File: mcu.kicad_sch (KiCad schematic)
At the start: 21 parts, among them J301 GPIO, SW301 RST, SW302 BOOT0, U301 STM32G0B1KBUx

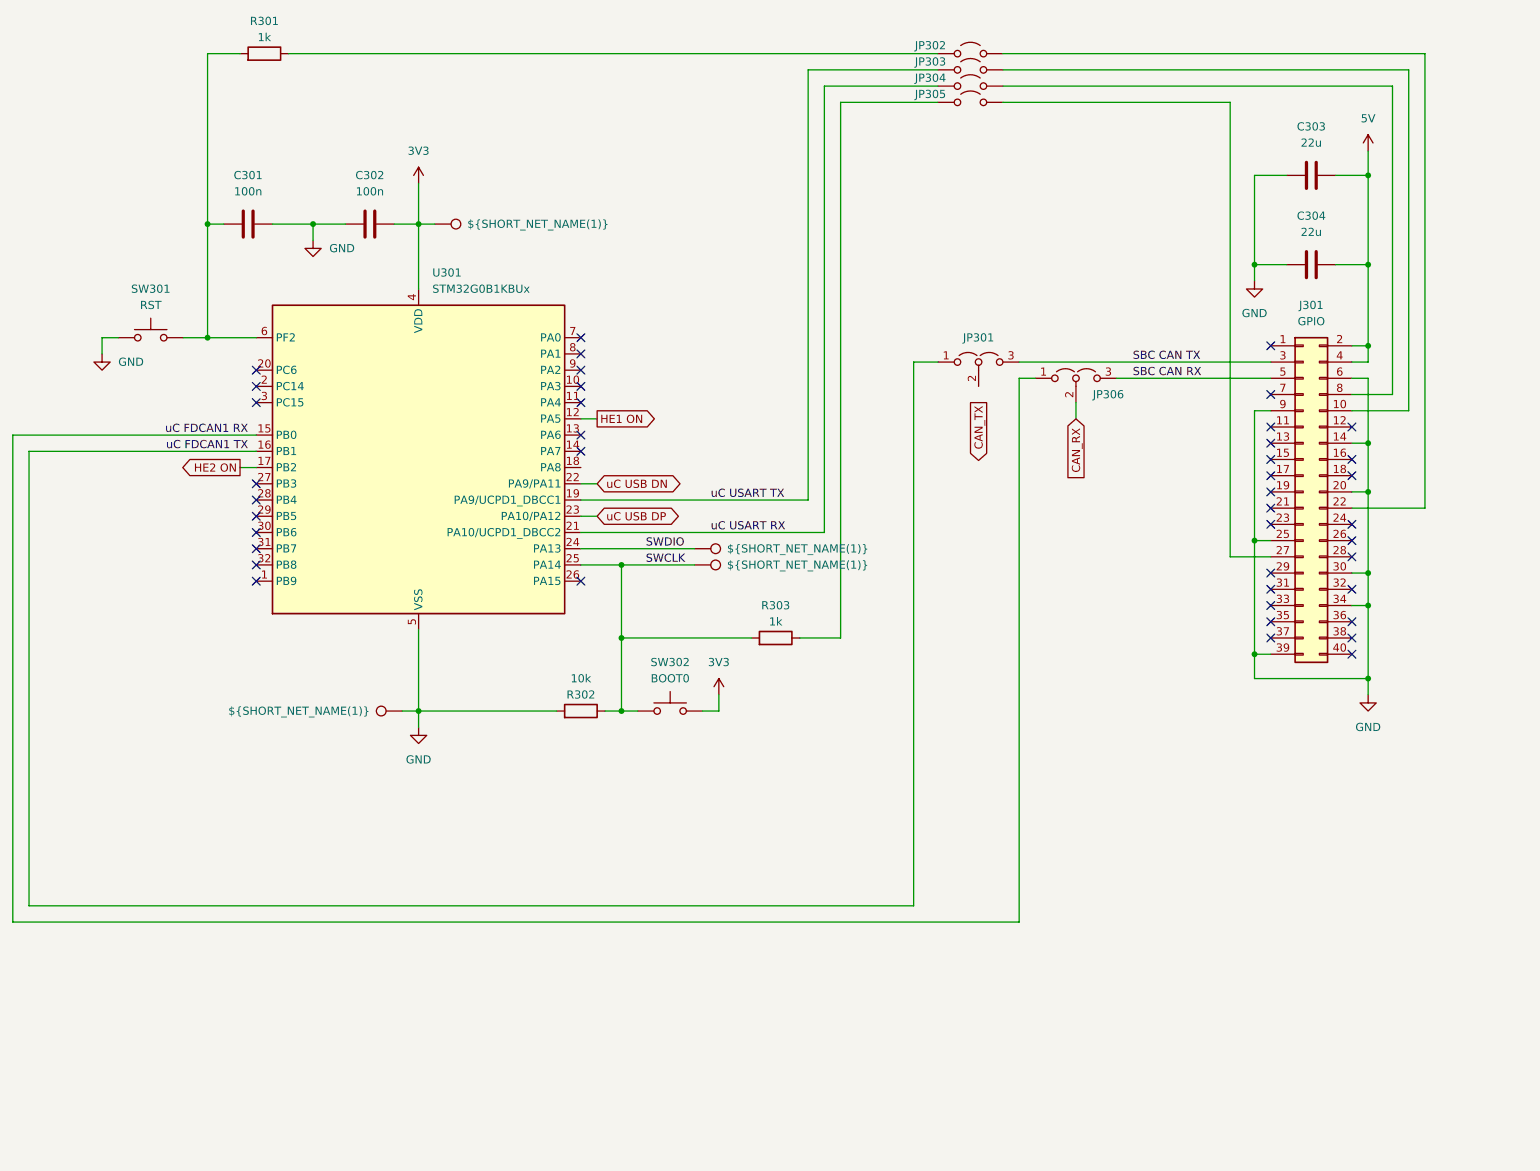
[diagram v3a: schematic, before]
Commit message: Schema improvements and CAN transceiver modification
- Improved schema layout for better readability and organization
- Connected CAN transceiver S-pin to GND for proper operation
- Updated PCB layout to reflect schema changes
- Enhanced component placement and routing clarity
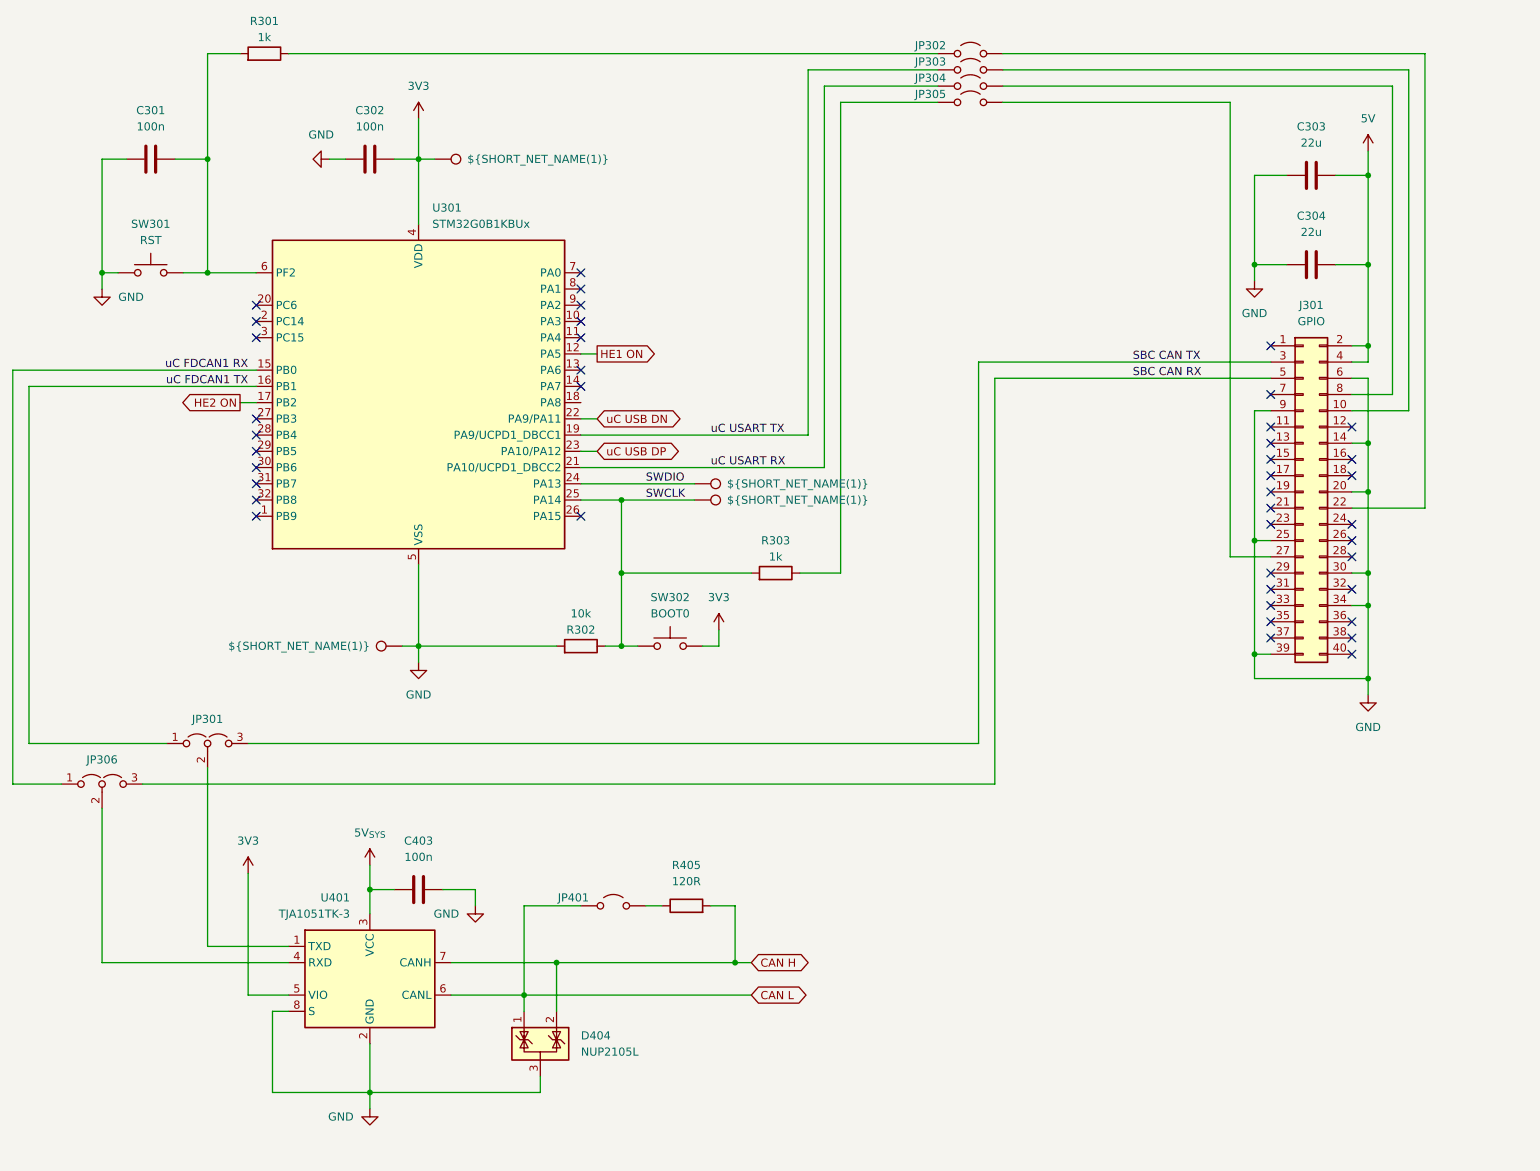
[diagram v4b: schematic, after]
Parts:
- added C403: 100n, Capacitor_SMD:C_0402_1005Metric, symbol Device:C
- added D404: NUP2105L, Package_TO_SOT_SMD:SOT-23, symbol Power_Protection:NUP2105L
- added JP401: ~, Connector_PinHeader_2.54mm:PinHeader_1x02_P2.54mm_Vertical, symbol Jumper:Jumper_2_Open
- added R405: 120R, Resistor_SMD:R_0402_1005Metric_Pad0.72x0.64mm_HandSolder, symbol Device:R
- added U401: TJA1051TK-3, Package_SON:HVSON-8-1EP_3x3mm_P0.65mm_EP1.6x2.4mm, symbol Interface_CAN_LIN:TJA1051TK-3
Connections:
- net 3V3: now also U401.5 (VIO)
- net GND: now also C403.1, D404.3 (A), U401.2 (GND), U401.8 (S), U401.9 (GND)
- net at JP301.2 (C): now also U401.1 (TXD)
- net CAN_RX: no longer names the net of JP306.2 (C)
- net CAN_RX: now also U401.4 (RXD)
- new net: JP401.2 (B), R405.1
- new net 5V_{SYS}: C403.2, U401.3 (VCC)
- new net CAN H: D404.2 (K), R405.2, U401.7 (CANH)
- new net CAN L: D404.1 (K), JP401.1 (A), U401.6 (CANL)
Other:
- moved on the sheet: C301, C302, JP301, JP306, R302, R303, SW301, SW302, U301

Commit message: Rev 0.2: Major hardware improvements and production readiness
Hardware Improvements (Thanks to shx for schematic cleanup):
- Clean up schematic organization and structure
- Set CAN transceiver Silent pin to GND for stability
- Add status LEDs (yellow: 24V/5V/3.3V, green: MCU PB4)
- Replace jumpers with solder jumpers on bottom side
- Add jumpers to output PFETs for permanent-on without firmware
- Add robust test points for 5V/GND load testing
- Add optional heatsink for DC/DC converter on bottom
- Add 10µF capacitor for MCU on 3.3V rail

Component Optimizations:
- Replace 30kΩ with 33kΩ basic part for simplified BOM
- Change DC/DC feedback: 15.5kΩ15kΩ (new output: 5.1V)
- Upgrade CAN ESD protection: NUP2105LPESD1CAN
- Increase CAN termination resistor footprint: 04020603
- Switch USB hub supply from 5V to 3.3V per datasheet

Production Ready:
- Add all LCSC part numbers and rotations
- Generate complete production data package
- Improve PCB layout and button placement
- Create comprehensive changelog documentation
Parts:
- removed TP302: ${SHORT_NET_NAME(1)}, project:NAMED_TEST_POINT, symbol project:NamedTestPoint
- added C303: 10u, Capacitor_SMD:C_0603_1608Metric, symbol Device:C
- added D301: GREEN, LED_SMD:LED_0805_2012Metric, symbol Device:LED
- added R301: 330R, Resistor_SMD:R_0402_1005Metric, symbol Device:R
- C301, C302: LCSC Part # (none) -> C307331; Manufacturer Part # (none) -> CL05B104KB54PNC
- C304: renamed from C403; LCSC Part # (none) -> C307331; Manufacturer Part # (none) -> CL05B104KB54PNC
- C305: renamed from C303; LCSC Part # (none) -> C12891; Manufacturer Part # (none) -> CL31A226KAHNNNE
- C306: renamed from C304; LCSC Part # (none) -> C12891; Manufacturer Part # (none) -> CL31A226KAHNNNE
- D302: renamed from D404; value NUP2105L -> PESD1CAN; LCSC Part # (none) -> C907838; Manufacturer Part # (none) -> PESD1CAN
- JP301: renamed from JP306; value Jumper_3_Open -> ~; footprint Connector_PinHeader_2.54mm:PinHeader_1x03_P2.54mm_Vertical -> project:SolderJumper-3_P1.3mm_Bridged12_RoundedPad1.0x1.5mm_custom; symbol Jumper:Jumper_3_Open -> Jumper:Jumper_3_Bridged12
- JP302: renamed from JP301; value Jumper_3_Open -> ~; footprint Connector_PinHeader_2.54mm:PinHeader_1x03_P2.54mm_Vertical -> project:SolderJumper-3_P1.3mm_Bridged12_RoundedPad1.0x1.5mm_custom; symbol Jumper:Jumper_3_Open -> Jumper:Jumper_3_Bridged12
- JP303: renamed from JP401; footprint Connector_PinHeader_2.54mm:PinHeader_1x02_P2.54mm_Vertical -> Jumper:SolderJumper-2_P1.3mm_Open_RoundedPad1.0x1.5mm; now left out of the parts list
- JP304: renamed from JP302; footprint Connector_PinHeader_2.54mm:PinHeader_1x02_P2.54mm_Vertical -> Jumper:SolderJumper-2_P1.3mm_Open_RoundedPad1.0x1.5mm; now left out of the parts list
- JP305: renamed from JP303; footprint Connector_PinHeader_2.54mm:PinHeader_1x02_P2.54mm_Vertical -> Jumper:SolderJumper-2_P1.3mm_Open_RoundedPad1.0x1.5mm; now left out of the parts list
- JP306: renamed from JP304; footprint Connector_PinHeader_2.54mm:PinHeader_1x02_P2.54mm_Vertical -> Jumper:SolderJumper-2_P1.3mm_Open_RoundedPad1.0x1.5mm; now left out of the parts list
- JP307: renamed from JP305; footprint Connector_PinHeader_2.54mm:PinHeader_1x02_P2.54mm_Vertical -> Jumper:SolderJumper-2_P1.3mm_Open_RoundedPad1.0x1.5mm; now left out of the parts list
- R302: renamed from R301; LCSC Part # (none) -> C11702; Manufacturer Part # (none) -> 0402WGF1001TCE
- R303: renamed from R302; LCSC Part # (none) -> C25744; Manufacturer Part # (none) -> 0402WGF1002TCE
- R304: renamed from R405; footprint Resistor_SMD:R_0402_1005Metric_Pad0.72x0.64mm_HandSolder -> Resistor_SMD:R_0603_1608Metric; LCSC Part # (none) -> C22787; Manufacturer Part # (none) -> 0603WAF1200T5E
- R305: renamed from R303; LCSC Part # (none) -> C11702; Manufacturer Part # (none) -> 0402WGF1001TCE
- SW301: value RST -> TS-1088; LCSC Part # (none) -> C720477; Manufacturer Part # (none) -> TS-1088-AR02016
- SW302: value BOOT0 -> TS-1088; LCSC Part # (none) -> C720477; Manufacturer Part # (none) -> TS-1088-AR02016
- TP301: now left out of the parts list
- TP302: renamed from TP303; now left out of the parts list
- TP303: renamed from TP304; now left out of the parts list
- U301: renamed from U401; LCSC Part # (none) -> C2875699; Manufacturer Part # (none) -> TJA1051TK/3/1J
- U302: renamed from U301; FT Rotation Offset (none) -> 270; LCSC Part # (none) -> C5159549; Manufacturer Part # (none) -> STM32G0B1KBU6
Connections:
- net 3V3: now also C303.1
- net GND: now also C303.2, D301.1 (K)
- net HE1 ON: now also U302.18 (PA8); no longer U302.12 (PA5)
- net at U302.28 (PB4): now also R301.1
- new net: D301.2 (A), R301.2
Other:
- moved on the sheet: C302

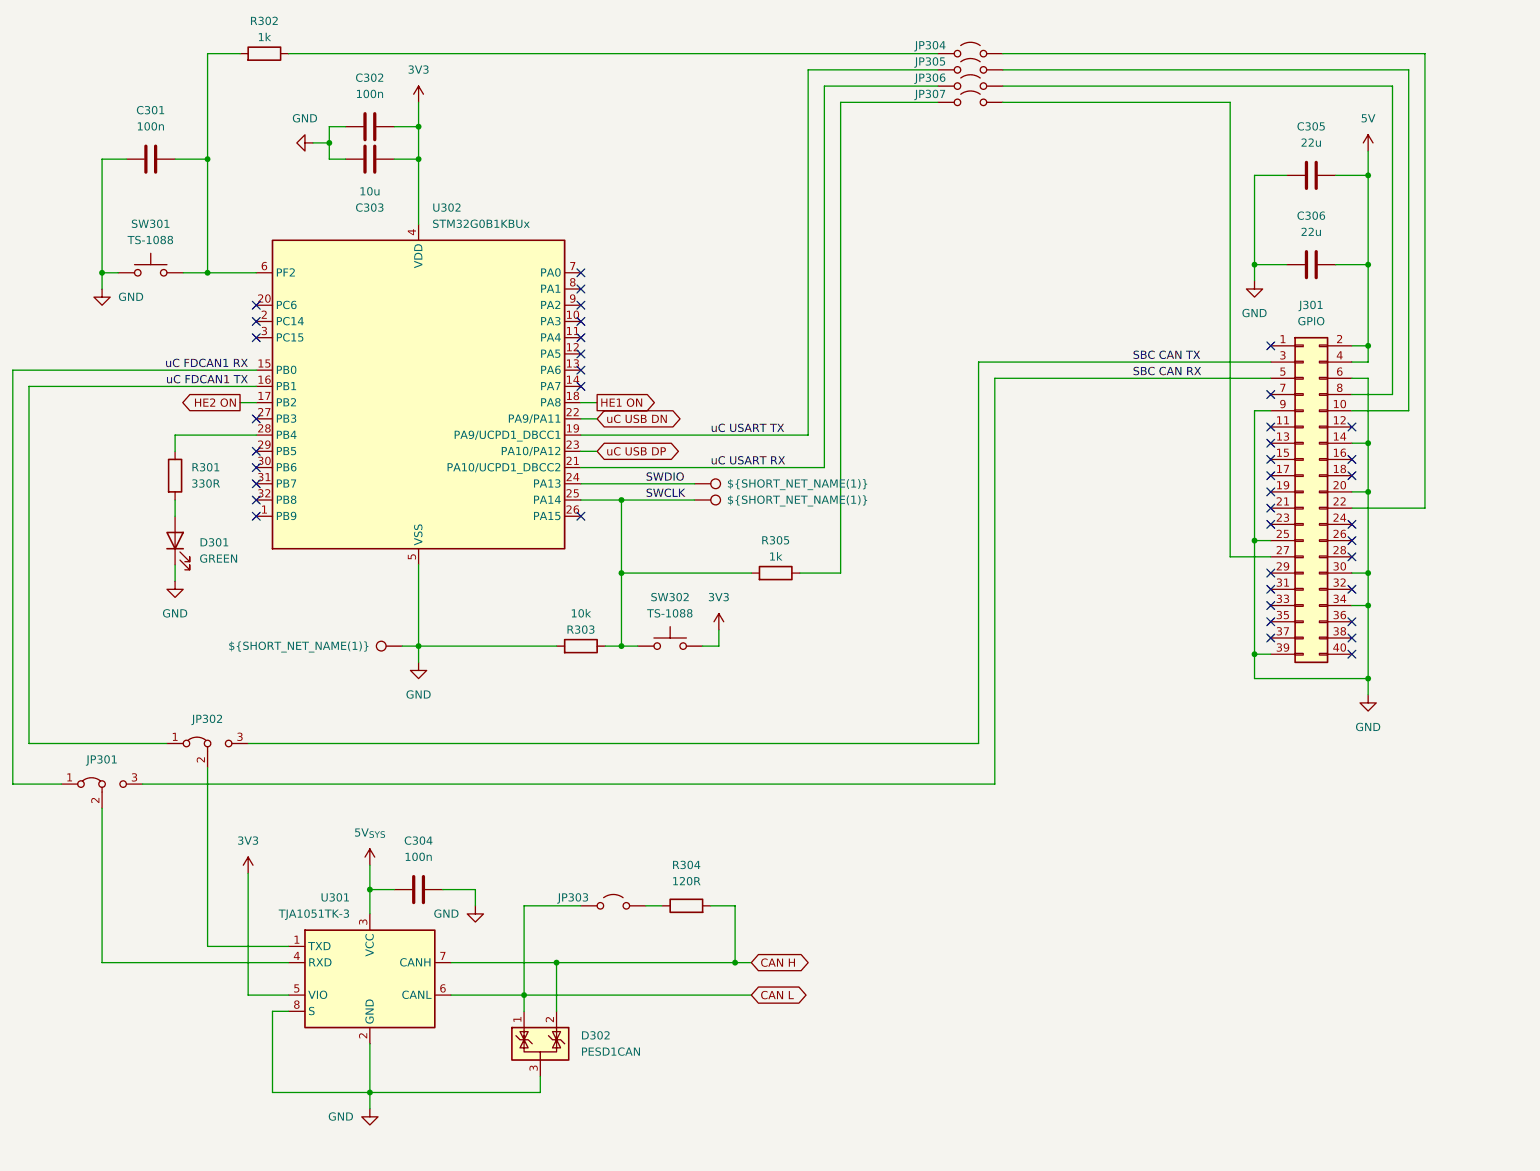
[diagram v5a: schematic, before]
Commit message: Rev. 0.3: Add 10µF capacitor C304 to CAN transceiver and QR code placeholder
- Added 10µF capacitor C304 for improved CAN communication stability
- Added QR code placeholder for serial number on PCB
- Enhanced signal integrity with additional filtering at CAN transceiver
- Improved traceability with unique identification capability
- Updated changelogs and documentation for Rev. 0.3
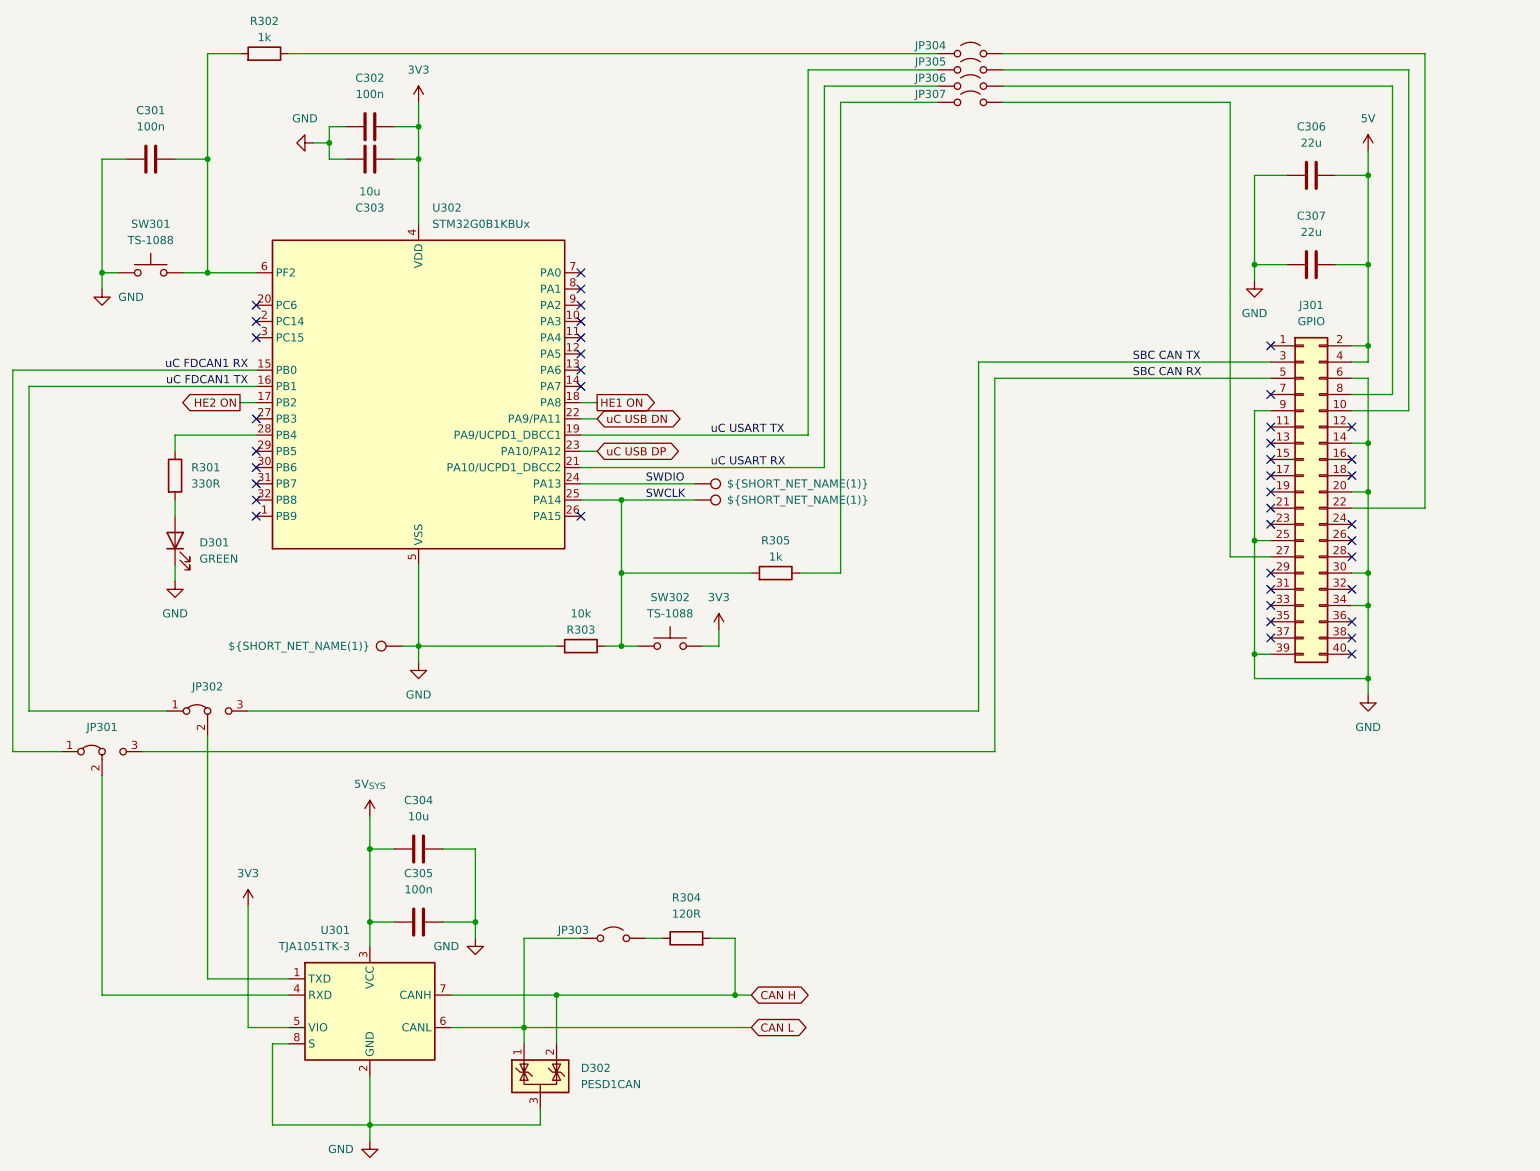
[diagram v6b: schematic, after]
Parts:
- added C304: 10u, Capacitor_SMD:C_0603_1608Metric, symbol Device:C
- renumbered C304 to C305, C305 to C306, C306 to C307
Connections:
- net 5V_{SYS}: now also C304.1
- net GND: now also C304.2
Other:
- moved on the sheet: C305, D302, JP301, JP302, JP303, R304, U301

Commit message: Production Optimization: JLCPCB assembly improvements
- Excluded test points TP202/TP203 from BOM
- Set FT rotation offsets for automated assembly:
  - U202/U301: 270° rotation offset
  - U401: 180° rotation offset
- Updated production data for JLCPCB compatibility
- Added unreleased changelog section for tracking
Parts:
- U301: FT Rotation Offset (none) -> 270
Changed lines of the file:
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@@
+			)
+		)
+		(property "FT Rotation Offset" "270"
+			(at 95.25 172.72 0)
+			(effects
+				(font
+					(size 1.27 1.27)
+				)
+				(hide yes)
 			)
 		)
